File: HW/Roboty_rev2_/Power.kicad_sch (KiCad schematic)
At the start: 14 parts, among them J3 USB_C_Receptacle_USB2.0, U2 NCP1117-3.3_SOT223, U3 USBLC6-2SC6

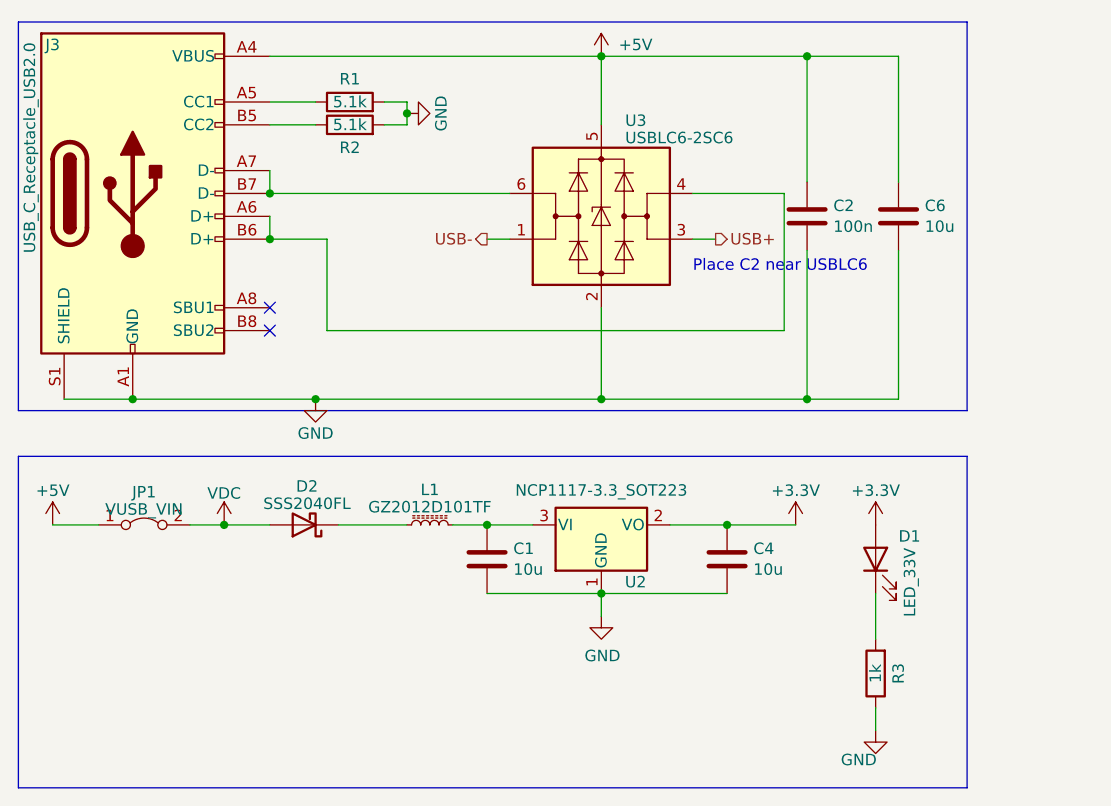
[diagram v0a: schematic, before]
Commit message: add sd card file library+ new HW version
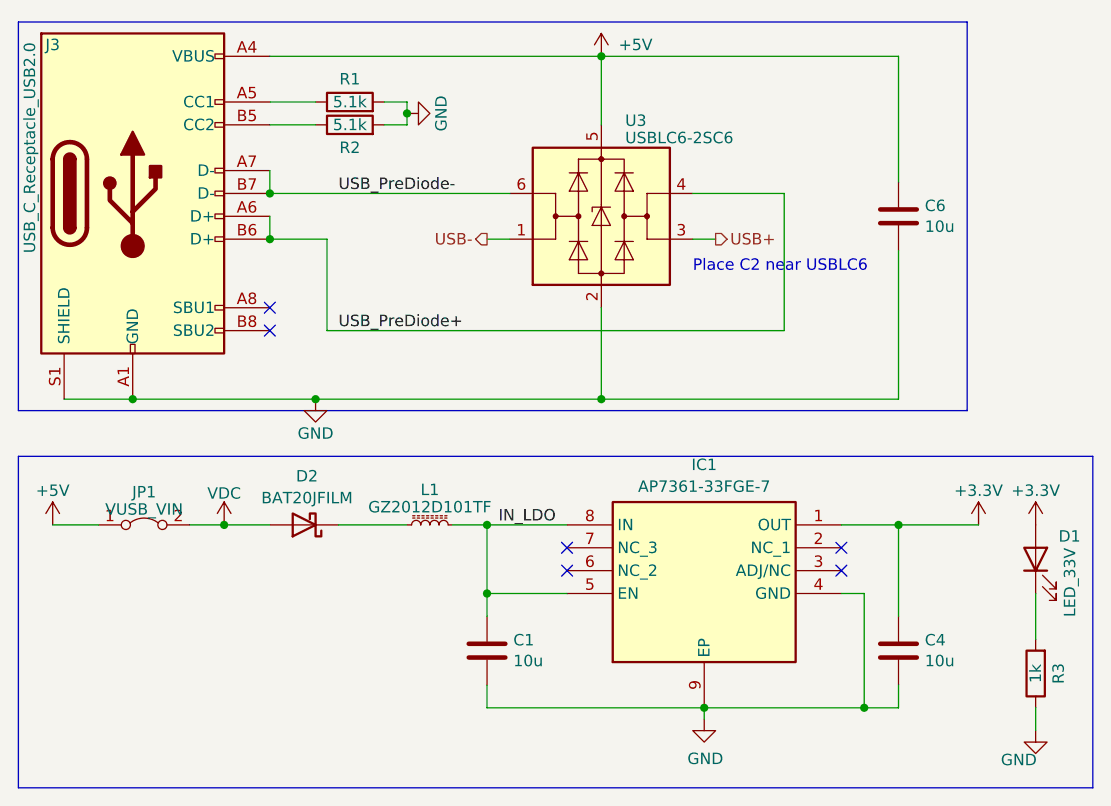
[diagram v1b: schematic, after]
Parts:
- removed C2: 100n, Capacitor_SMD:C_0603_1608Metric, symbol Device:C
- removed U2: NCP1117-3.3_SOT223, Package_TO_SOT_SMD:SOT-223-3_TabPin2, symbol Regulator_Linear:NCP1117-3.3_SOT223
- added IC1: AP7361-33FGE-7, Package_SON:VSON-8-1EP_3x3mm_P0.65mm_EP1.65x2.4mm, symbol AREA_composant:AP7361-33FGE-7
- D2: value SSS2040FL -> BAT20JFILM; footprint Diode_SMD:D_SOD-123 -> Diode_SMD:D_SOD-323
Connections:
- net +3V3: now also IC1.1 (OUT)
- net GND: now also IC1.4 (GND), IC1.9 (EP)
- net USB_PreDiode+: now reaches J3.A6 (D+), J3.B6 (D+), U3.4 (I/O2)
- net USB_PreDiode-: now reaches J3.A7 (D-), J3.B7 (D-), U3.6 (I/O1)
- net IN_LDO: now reaches C1.1, L1.2
- net IN_LDO: now also IC1.5 (EN), IC1.8 (IN)
- no-connect marks 2 -> 6
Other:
- moved on the sheet: C1, C4, D1, R3
